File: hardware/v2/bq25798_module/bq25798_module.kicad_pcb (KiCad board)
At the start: 4 copper layers, 81.1 x 68.6 mm, 51 parts, among them IC1 BQ25798RQMR, J1 Input 12V DC, J2 Output 12V DC, J3 Battery, J5 I2C (no pullups), J6 NTC temp sensor, Q1 AON7528, Q2 AON7528

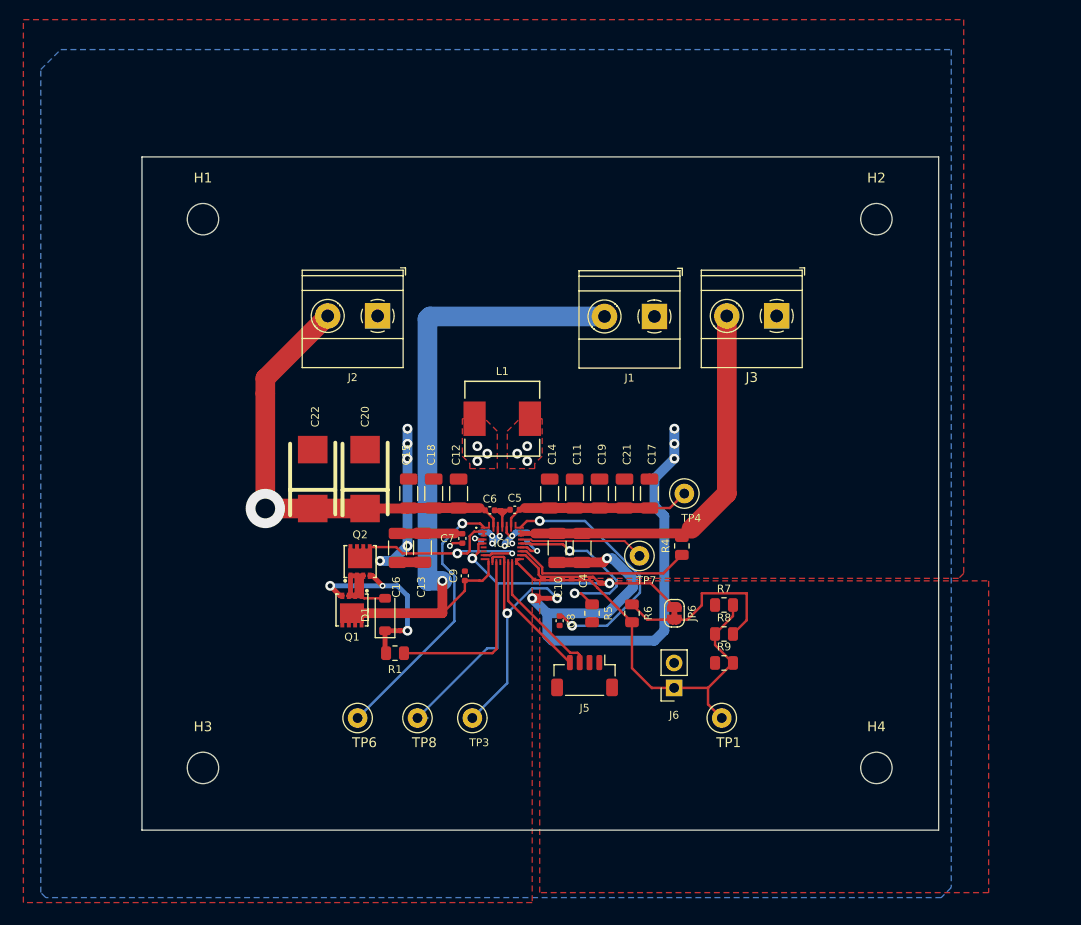
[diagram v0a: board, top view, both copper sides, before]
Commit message: update board to v2.1
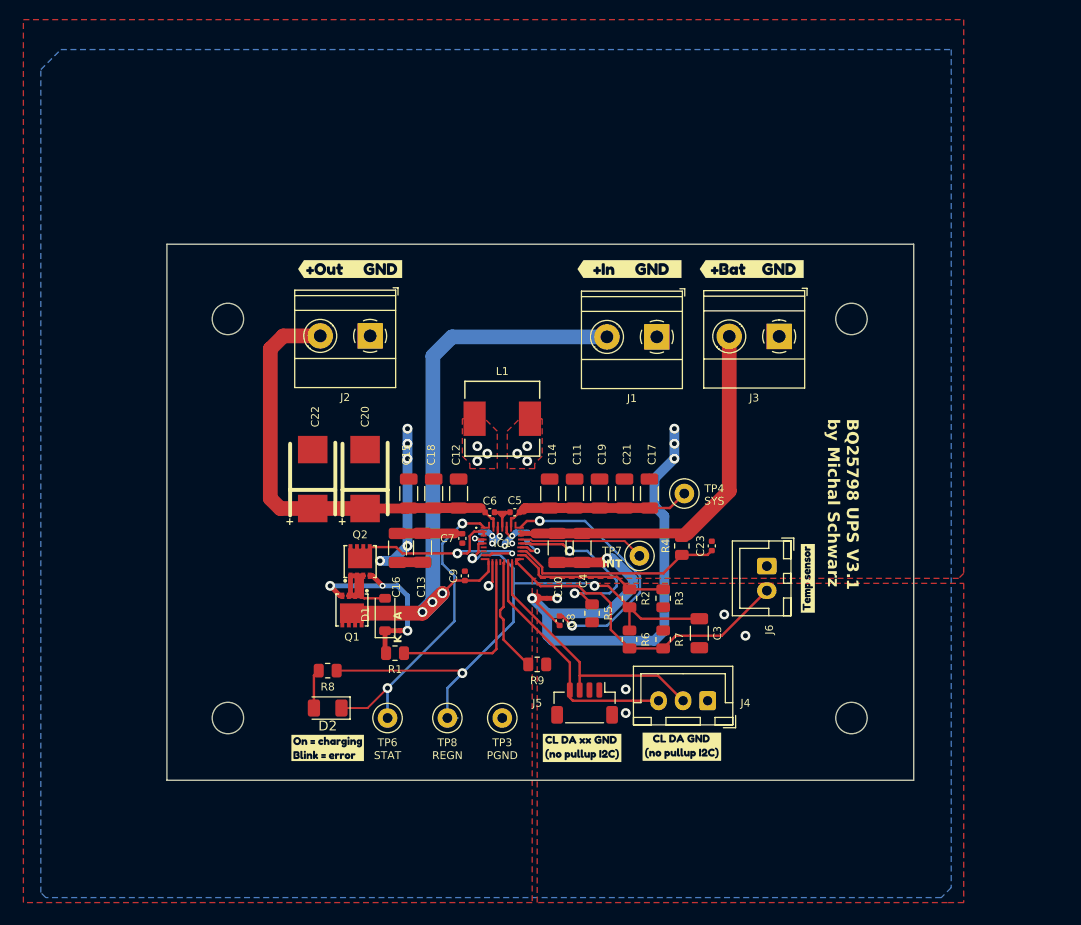
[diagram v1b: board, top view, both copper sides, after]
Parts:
- removed JP6: Temp simul, Jumper:SolderJumper-2_P1.3mm_Bridged_RoundedPad1.0x1.5mm
- removed NT3: ~, NetTie:NetTie-2_SMD_Pad0.5mm
- removed TP1: TS, TestPoint:TestPoint_Loop_D1.80mm_Drill1.0mm_Beaded
- added C23: 47n 25V, Capacitor_SMD:C_0402_1005Metric, F.Cu at (110.2, 68.8)
- added C3: 4.7u 10V, Capacitor_SMD:C_1206_3216Metric, F.Cu at (109.0, 77.7)
- added D2: LED, LED_SMD:LED_1206_3216Metric, F.Cu at (71.1, 85.3)
- added J4: I2C, Connector_JST:JST_XH_B3B-XH-A_1x03_P2.50mm_Vertical, F.Cu at (109.8, 84.6)
- added R2: 1R, Resistor_SMD:R_0805_2012Metric, F.Cu at (101.9, 74.2)
- added R3: 1M, Resistor_SMD:R_0805_2012Metric, F.Cu at (105.3, 74.2)
- added kibuzzard-680F50CE: G***, kibuzzard-680F50CE, F.Cu at (101.9, 40.6)
- added kibuzzard-680F50E1: G***, kibuzzard-680F50E1, F.Cu at (114.3, 40.6)
- added kibuzzard-680F50F5: G***, kibuzzard-680F50F5, F.Cu at (73.4, 40.6)
- added kibuzzard-680F5553: G***, kibuzzard-680F5553, F.Cu at (71.1, 89.4)
- added kibuzzard-680F5C84: G***, kibuzzard-680F5C84, F.Cu at (97.0, 89.4)
- added kibuzzard-680FCC32: G***, kibuzzard-680FCC32, F.Cu at (120.0, 72.1)
- added kibuzzard-680FCE97: G***, kibuzzard-680FCE97, F.Cu at (107.2, 89.3)
- C1, C2: value 47n 10V -> 47n 25V
- C10, C11, C12, C13, C14, C15, C16, C17, C18, C19, C21, C4: value 10u -> 10u 25V
- C5, C6, C7, C9: value 100n -> 100n 25V
- C8: value 1nF, 50V, 0402 package -> 1nF, 50V
- J5: value I2C (no pullups) -> I2C QWIIC/uŠup
- J6: footprint Connector_PinSocket_2.54mm:PinSocket_1x02_P2.54mm_Vertical -> Connector_JST:JST_XH_B2B-XH-A_1x02_P2.50mm_Vertical
- NT1: value grounds -> ~
- R8: value ? -> 2k2
- TP3: value GND -> PGND
- TP6: value Charge status (OD) -> STAT
- TP7: value Interrupt (OD) -> INT
- TP8: value REGN LDO -> REGN
- moved R8 40.5 mm to (71.1, 81.5), turned to 180 degrees
- moved R9 19.0 mm to (92.5, 80.9), turned to 180 degrees
- moved J6 15.6 mm to (115.8, 70.9), turned to -90 degrees
- moved H2 10.5 mm to (124.5, 45.7)
- moved H1 10.5 mm to (61.0, 45.7)
- moved R7 7.12 mm to (105.3, 78.4), turned to -90 degrees
- moved H4 5.68 mm to (124.5, 86.4)
- moved H3 5.68 mm to (61.0, 86.4)
- moved TP3 3.05 mm to (88.9, 86.4)
- moved TP8 3.05 mm to (83.3, 86.4)
- moved TP6 3.05 mm to (77.2, 86.4)
- moved J5 2.79 mm to (97.3, 84.8)
- moved R6 2.68 mm to (101.9, 78.4)
- moved J2 2.17 mm to (75.4, 47.4)
- moved J1 2.10 mm to (104.6, 47.5)
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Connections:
- C8 pad 2: GND -> PGND
- IC1 pad 10: GND -> PGND
- IC1 pad 13: GND -> Net-(IC1-~{CE})
- J6 pad 1: TS -> GND
- J6 pad 2: GND -> TS
- R6 pad 1: Net-(JP6-B) -> REGN
- R8 pad 1: TS -> REGN
- R8 pad 2: Net-(JP6-B) -> Net-(D2-A)
- R9 pad 2: TS -> Net-(IC1-~{CE})
- TP3 pad 1: GND -> PGND
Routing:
- net GND: track 27.2 -> 1.16 mm, vias 2 -> 5
- net Net-(JP6-B): track 18.9 -> 0.00 mm
- net REGN: track 43.6 -> 61.9 mm, vias 2 -> 3
- net I2C_SDA: track 13.5 -> 27.5 mm
- net SYS: track 33.7 -> 21.0 mm
- net I2C_SCL: track 12.8 -> 25.6 mm
- net Net-(IC1-~{CE}): track 0.00 -> 11.8 mm
- net TS: track 42.8 -> 33.8 mm
- net ILIM_HIZ: track 9.63 -> 16.4 mm
- net PGND: track 87.6 -> 93.5 mm
- net STAT: track 27.7 -> 31.9 mm, vias 1 -> 2
- net Net-(D2-A): track 0.00 -> 4.01 mm
- net BATTERY: track 42.5 -> 39.2 mm
- net Net-(IC1-BATP): track 18.5 -> 21.7 mm
- net VIN1: track 67.1 -> 64.6 mm, vias 1 -> 3
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- added copper zone on In2.Cu, net GND
- added copper zone on In1.Cu, net PGND
- removed copper zone on In2.Cu, net PMID
- removed copper zone on In1.Cu, net VBUS
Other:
- board size 81.1 x 68.6 mm -> 76 x 54.6 mm
- board text added: "+"
- board text added: "BQ25798 UPS V3.1 by Michal Schwarz"
- board text added: "INT"
- board text added: "K A"

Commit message: wip
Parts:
- removed J5: I2C QWIIC/uŠup, Connector_JST:JST_SH_BM04B-SRSS-TB_1x04-1MP_P1.00mm_Vertical
- removed kibuzzard-680F5C84: G***, kibuzzard-680F5C84
- removed kibuzzard-680FCE97: G***, kibuzzard-680FCE97
- added C24: 47u low ESR, Capacitor_SMD:C_Elec_6.3x5.8, F.Cu at (62.9, 56.4)
- added C25: 47u low ESR, Capacitor_SMD:C_Elec_6.3x5.8, F.Cu at (62.9, 65.0)
- added kibuzzard-680FE071: G***, kibuzzard-680FE071, F.Cu at (97.9, 89.4)
- C10, C11, C12, C13, C14, C15, C16, C17, C18, C19, C21, C3, C4: footprint Capacitor_SMD:C_1206_3216Metric -> Capacitor_SMD:C_0805_2012Metric
- L1: footprint snapeda:INDM7676X435N -> Inductor_SMD:L_12x12mm_H6mm
- moved kibuzzard-680FCC32 19.3 mm to (110.5, 88.9), turned to 0 degrees
- moved J6 14.4 mm to (111.7, 84.7), turned to 180 degrees
- moved C17 13.7 mm to (90.2, 63.0)
- moved J4 9.40 mm to (100.4, 84.7)
- moved C15 8.27 mm to (87.6, 63.0)
- moved R9 3.68 mm to (89.9, 78.2), turned to 90 degrees
- moved L1 1.52 mm to (88.9, 54.4)
- moved C11 1.27 mm to (95.0, 63.5)
- moved C21 1.27 mm to (100.1, 63.5)
- moved C14 1.27 mm to (92.5, 63.5)
- moved C18 1.27 mm to (83.2, 63.5)
- moved C19 1.27 mm to (97.5, 63.5)
- moved C12 1.02 mm to (85.5, 63.5)
- moved C22 0.76 mm to (70.4, 62.0)
- moved C20 0.76 mm to (75.7, 62.0)
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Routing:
- net I2C_SDA: track 27.5 -> 17.6 mm
- net PGND: track 93.5 -> 84.3 mm, vias 11 -> 15
- net I2C_SCL: track 25.6 -> 16.7 mm
- net TS: track 33.8 -> 27.9 mm
- net VIN1: track 64.6 -> 70.4 mm, vias 3 -> 8
- net Net-(IC1-~{CE}): track 11.8 -> 7.24 mm
- net GND: track 1.16 -> 4.06 mm, vias 5 -> 2
- net Net-(IC1-VAC2): track 22.9 -> 25.8 mm, vias 2 -> 7
- net SW1: track 18.1 -> 20.4 mm
- net SYS: track 21.0 -> 22.8 mm
- net PMID: track 55.2 -> 56.9 mm
- net REGN: track 61.9 -> 60.3 mm
- net BTST2: track 3.24 -> 2.60 mm

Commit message: v2.1 final
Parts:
- removed TP6: STAT, TestPoint:TestPoint_Loop_D1.80mm_Drill1.0mm_Beaded
- removed TP7: INT, TestPoint:TestPoint_Loop_D1.80mm_Drill1.0mm_Beaded
- removed kibuzzard-680FE071: G***, kibuzzard-680FE071
- added NT4: ~, NetTie:NetTie-2_SMD_Pad0.5mm, F.Cu at (84.7, 69.7)
- added TP1: GND, TestPoint:TestPoint_Loop_D1.80mm_Drill1.0mm_Beaded, F.Cu at (114.3, 76.0)
- added kibuzzard-6810EFE9: G***, kibuzzard-6810EFE9, F.Cu at (104.1, 90.2)
- added kibuzzard-6810F062: G***, kibuzzard-6810F062, F.Cu at (94.0, 90.2)
- added kibuzzard-6810F0BF: G***, kibuzzard-6810F0BF, F.Cu at (106.7, 90.2)
- added kibuzzard-6810F0CD: G***, kibuzzard-6810F0CD, F.Cu at (101.6, 89.9)
- added kibuzzard-6810F0D5: G***, kibuzzard-6810F0D5, F.Cu at (96.5, 89.9)
- C3: moved to B.Cu
- D2: footprint LED_SMD:LED_1206_3216Metric -> LED_SMD:LED_0805_2012Metric
- J4: value I2C -> Controller Connection; footprint Connector_JST:JST_XH_B3B-XH-A_1x03_P2.50mm_Vertical -> Connector_JST:JST_XH_B6B-XH-A_1x06_P2.50mm_Vertical
- moved C3 21.2 mm to (88.5, 72.3)
- moved C8 10.2 mm to (93.5, 66.3), turned to 0 degrees
- moved J4 6.10 mm to (106.5, 84.7)
- moved R5 4.22 mm to (94.0, 74.5), turned to 0 degrees
- moved NT1 3.99 mm to (96.9, 74.8)
- moved J6 3.81 mm to (115.5, 84.7)
- moved kibuzzard-680FCC32 3.81 mm to (114.3, 88.9)
- moved TP8 3.30 mm to (80.0, 86.4)
- moved TP3 2.54 mm to (86.4, 86.4)
- moved TP4 2.03 mm to (105.4, 63.5)
- moved C16 1.70 mm to (79.6, 68.1)
- moved C13 1.48 mm to (81.9, 68.1)
- moved C9 1.17 mm to (84.8, 70.7), turned to 180 degrees
- moved C10 0.25 mm to (94.2, 68.7)
- moved C4 0.25 mm to (97.2, 68.7)
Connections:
- net I2C_SCL renamed Net-(IC1-SCL)
- net I2C_SDA renamed Net-(IC1-SDA)
- IC1 pad 10: PGND -> GND
- IC1 pad 21: ~{INT} -> Net-(IC1-~{INT})
- Q2 pad 5: Net-(IC1-VAC2) -> Net-(NT4-Pad2)
- Q2 pad 6: Net-(IC1-VAC2) -> Net-(NT4-Pad2)
- Q2 pad 7: Net-(IC1-VAC2) -> Net-(NT4-Pad2)
- Q2 pad 8: Net-(IC1-VAC2) -> Net-(NT4-Pad2)
- Q2 pad 9: Net-(IC1-VAC2) -> Net-(NT4-Pad2)
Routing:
- net PGND: track 84.3 -> 5.03 mm, vias 15 -> 33
- net Net-(IC1-~{INT}): track 0.00 -> 29.2 mm, vias 0 -> 1
- net SDRV: track 26.5 -> 2.27 mm, vias 2 -> 0
- net Net-(IC1-VAC2): track 25.8 -> 6.27 mm, vias 7 -> 0
- net Net-(NT4-Pad2): track 0.00 -> 13.2 mm
- net ~{INT}: track 12.8 -> 0.00 mm
- net Net-(IC1-~{CE}): track 7.24 -> 18.5 mm
- net PMID: track 56.9 -> 45.9 mm
- net Net-(IC1-PROG): track 18.8 -> 9.37 mm
- net REGN: track 60.3 -> 53.4 mm
- net SW2: track 20.5 -> 26.5 mm
- net GND: track 4.06 -> 8.77 mm, vias 2 -> 7
- net Net-(IC1-SDA): track 17.6 -> 21.4 mm
- net Net-(D1-K): track 19.9 -> 23.5 mm, vias 3 -> 2
- net SW1: track 20.4 -> 24.0 mm
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- added copper zone on B.Cu, net PGND
- removed copper zone on B.Cu, net GND
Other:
- board size 76 x 54.6 mm -> 76 x 55.9 mm

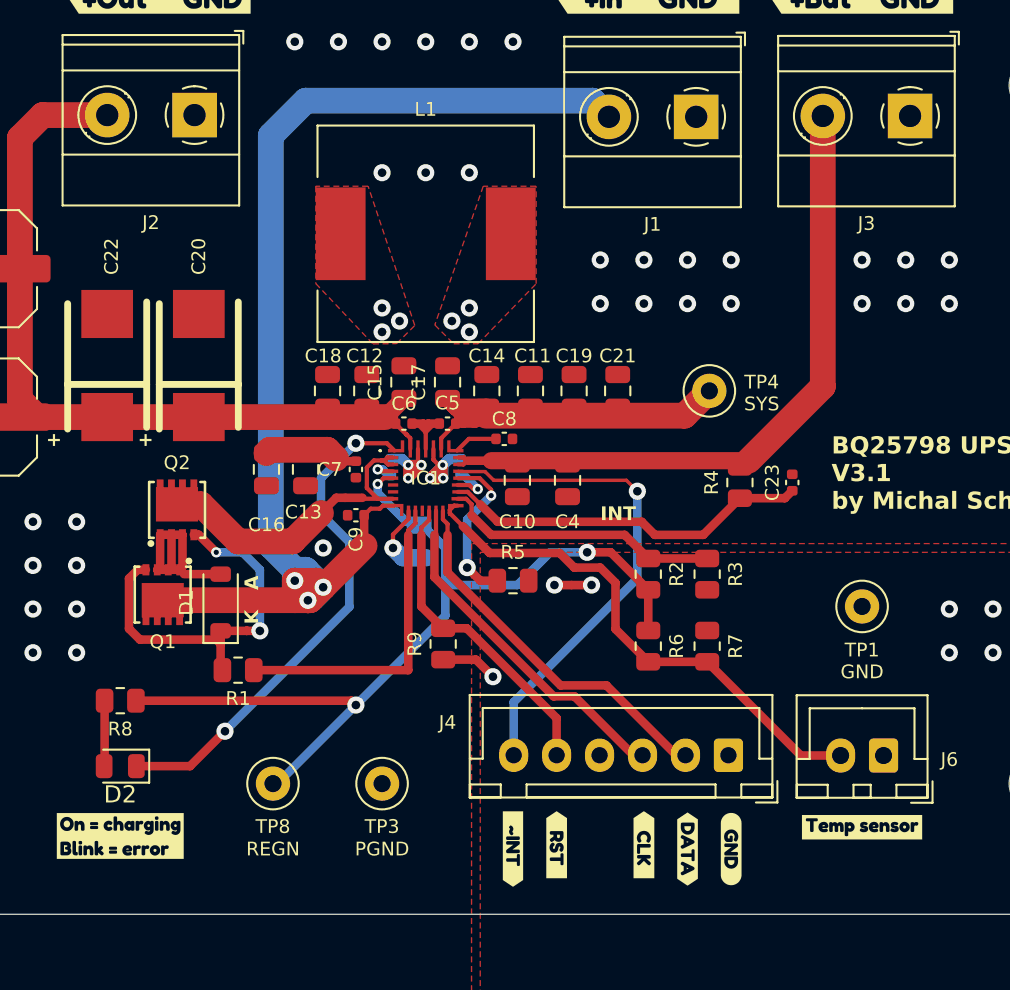
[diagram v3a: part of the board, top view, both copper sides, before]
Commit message: add thermal reliefs, simplify PCB
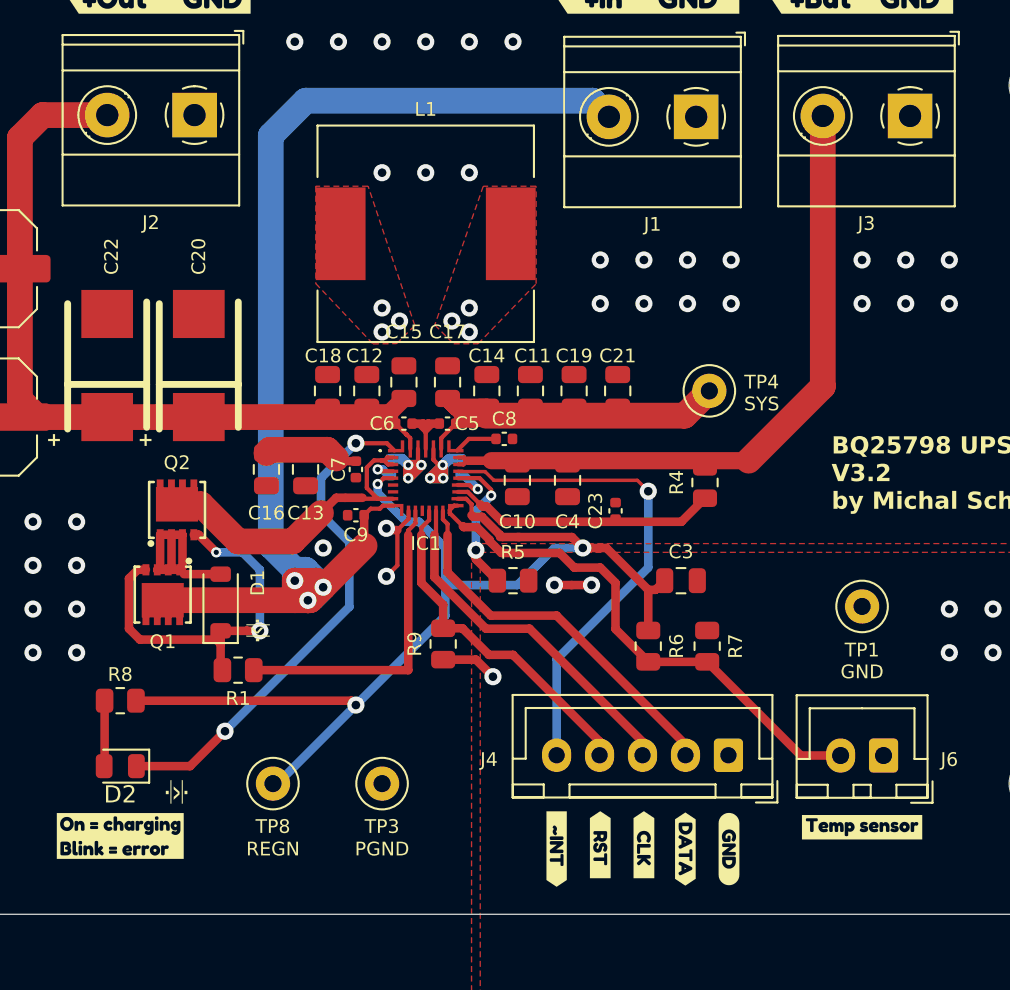
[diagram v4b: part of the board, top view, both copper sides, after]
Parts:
- removed R2: 1R, Resistor_SMD:R_0805_2012Metric
- removed R3: 1M, Resistor_SMD:R_0805_2012Metric
- added NT2: ~, NetTie:NetTie-2_SMD_Pad0.5mm, F.Cu at (93.9, 72.0)
- C3: moved to F.Cu
- J4: footprint Connector_JST:JST_XH_B6B-XH-A_1x06_P2.50mm_Vertical -> Connector_JST:JST_XH_B5B-XH-A_1x05_P2.50mm_Vertical
- moved C3 15.4 mm to (103.8, 74.5), turned to 0 degrees
- moved C23 10.4 mm to (99.9, 70.5)
- moved kibuzzard-6810F0D5 2.54 mm to (99.1, 89.9)
- moved kibuzzard-6810F062 2.54 mm to (96.5, 90.2)
- moved R4 2.03 mm to (105.2, 68.8)
- moved kibuzzard-6810F0BF 0.13 mm to (106.6, 90.2)
- moved kibuzzard-6810EFE9 0.13 mm to (104.0, 90.2)
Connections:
- J4 pad 4: unconnected-(J4-Pin_4-Pad4) -> Net-(IC1-~{CE})
- J4 pad 5: Net-(IC1-~{CE}) -> Net-(IC1-~{INT})
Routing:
- net ILIM_HIZ: track 16.4 -> 3.85 mm
- net Net-(IC1-BATP): track 21.6 -> 15.7 mm
- net REGN: track 53.4 -> 58.8 mm
- net Net-(IC1-~{CE}): track 18.5 -> 20.4 mm
- net Net-(IC1-SDA): track 21.4 -> 22.9 mm
- net Net-(IC1-PROG): track 9.37 -> 8.37 mm
- net Net-(IC1-SCL): track 19.8 -> 20.8 mm
- net GND: track 8.77 -> 9.49 mm, vias 7 -> 8
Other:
- board text added: "-|<|-"
- board text added: "BQ25798 UPS V3.2 by Michal Schwarz"
- board text removed: "BQ25798 UPS V3.1 by Michal Schwarz"
- board text removed: "INT"
- board text removed: "K A"

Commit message: add power output to the J4
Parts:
- added kibuzzard-683C9D12: G***, kibuzzard-683C9D12, F.Cu at (106.4, 89.9)
- J4: value Controller Connection -> Conn_01x06_Pin; footprint Connector_JST:JST_XH_B5B-XH-A_1x05_P2.50mm_Vertical -> Connector_JST:JST_XH_B6B-XH-A_1x06_P2.50mm_Vertical
- moved kibuzzard-6810EFE9 2.54 mm to (101.5, 90.2)
- moved kibuzzard-6810F0D5 2.54 mm to (96.5, 89.9)
- moved kibuzzard-6810F062 2.54 mm to (94.0, 90.2)
- moved kibuzzard-6810F0BF 2.54 mm to (104.0, 90.2)
- moved kibuzzard-6810F0CD 2.54 mm to (99.1, 89.9)
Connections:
- IC1 pad 13: Net-(IC1-~{CE}) -> /~RST
- IC1 pad 14: Net-(IC1-SCL) -> /I2C_SCL
- IC1 pad 15: Net-(IC1-SDA) -> /I2C_SDA
- IC1 pad 21: Net-(IC1-~{INT}) -> /~INT
- J4 pad 1: GND -> PMID
- J4 pad 2: Net-(IC1-SDA) -> GND
- J4 pad 3: Net-(IC1-SCL) -> /I2C_SDA
- J4 pad 4: Net-(IC1-~{CE}) -> /I2C_SCL
- J4 pad 5: Net-(IC1-~{INT}) -> /~RST
- R9 pad 2: Net-(IC1-~{CE}) -> /~RST
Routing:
- net PMID: track 45.9 -> 110.5 mm
- net /~INT: track 0.00 -> 30.1 mm, vias 0 -> 1
- net Net-(IC1-~{INT}): track 29.1 -> 0.00 mm, vias 1 -> 0
- net Net-(IC1-SDA): track 22.9 -> 0.00 mm
- net Net-(IC1-SCL): track 20.8 -> 0.00 mm
- net Net-(IC1-~{CE}): track 20.4 -> 0.00 mm
- net /I2C_SDA: track 0.00 -> 20.3 mm
- net /I2C_SCL: track 0.00 -> 19.6 mm
- net /~RST: track 0.00 -> 18.8 mm
- net GND: track 9.49 -> 10.7 mm
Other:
- board text added: "BQ25798 UPS V3.3 by Michal Schwarz"
- board text removed: "BQ25798 UPS V3.2 by Michal Schwarz"

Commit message: wip ESP32 schematics
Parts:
- removed kibuzzard-683C9D12: G***, kibuzzard-683C9D12
- added C26: 470u 50V, Capacitor_SMD:C_0805_2012Metric, F.Cu at (128.3, 101.0)
- added C27: 220u 25V, Capacitor_SMD:C_0805_2012Metric, F.Cu at (128.3, 94.0)
- added C28: 10u 25V, Capacitor_SMD:C_0805_2012Metric, F.Cu at (137.2, 52.7)
- added J5: USB_C_Receptacle_USB2.0_14P, Connector_USB:USB_C_Receptacle_HCTL_HC-TYPE-C-16P-01A, F.Cu at (103.2, 97.2)
- added L2: 68 uH, mouser (samacsys):INDPM7676X435N, F.Cu at (133.3, 97.2)
- added R2: 5k1, Resistor_SMD:R_0805_2012Metric, F.Cu at (134.9, 79.4)
- added R3: 5k1, Resistor_SMD:R_0805_2012Metric, F.Cu at (134.9, 82.5)
- added U1: ESP32-S2-WROVER, RF_Module:ESP32-S2-WROVER, F.Cu at (126.4, 64.1)
- added U2: LM2596S-3.3, Package_TO_SOT_SMD:TO-263-5_TabPin3, F.Cu at (116.4, 96.5)
- added kibuzzard-68570239: G***, kibuzzard-68570239, F.Cu at (106.4, 89.9)
